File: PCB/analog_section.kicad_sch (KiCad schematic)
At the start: 75 parts, among them J3 Probe +, J4 Probe +, J5 Probe -, J6 Probe -, U1 TLV757P, U10 LM324, U3 AD9833xRM, U4 LMH6643MMX, U6 LMH6643MMX, U7 LMH6643MMX, Y1 25MHz

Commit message: Fixed some PCB bugs
The OLED display ribbon cable folded the wrong way so the screen faced
down, so I fixed that. Also made vias untented, made diodes
easier to hand solder, and added ground test hook.
The case CAD still needs to be updated.
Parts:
- D3, D4, D7, D9: footprint Diode_SMD:D_SOD-323F -> Diode_SMD:D_SOD-323_HandSoldering
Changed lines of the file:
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@@
 	(title_block
 		(title "LCR Analog Section")
-		(date "2026-05-16")
+		(date "2026-06-03")
 		(company "LWQ")
 	)
@@
 			)
 		)
-		(property "Footprint" "Diode_SMD:D_SOD-323F"
+		(property "Footprint" "Diode_SMD:D_SOD-323_HandSoldering"
 			(at 359.41 176.53 0)
 			(hide yes)
@@
 			)
 		)
-		(property "Footprint" "Diode_SMD:D_SOD-323F"
+		(property "Footprint" "Diode_SMD:D_SOD-323_HandSoldering"
 			(at 359.41 219.71 0)
 			(hide yes)
@@
 			)
 		)
-		(property "Footprint" "Diode_SMD:D_SOD-323F"
+		(property "Footprint" "Diode_SMD:D_SOD-323_HandSoldering"
 			(at 359.41 232.41 0)
 			(hide yes)
@@
 			)
 		)
-		(property "Footprint" "Diode_SMD:D_SOD-323F"
+		(property "Footprint" "Diode_SMD:D_SOD-323_HandSoldering"
 			(at 359.41 163.83 0)
 			(hide yes)

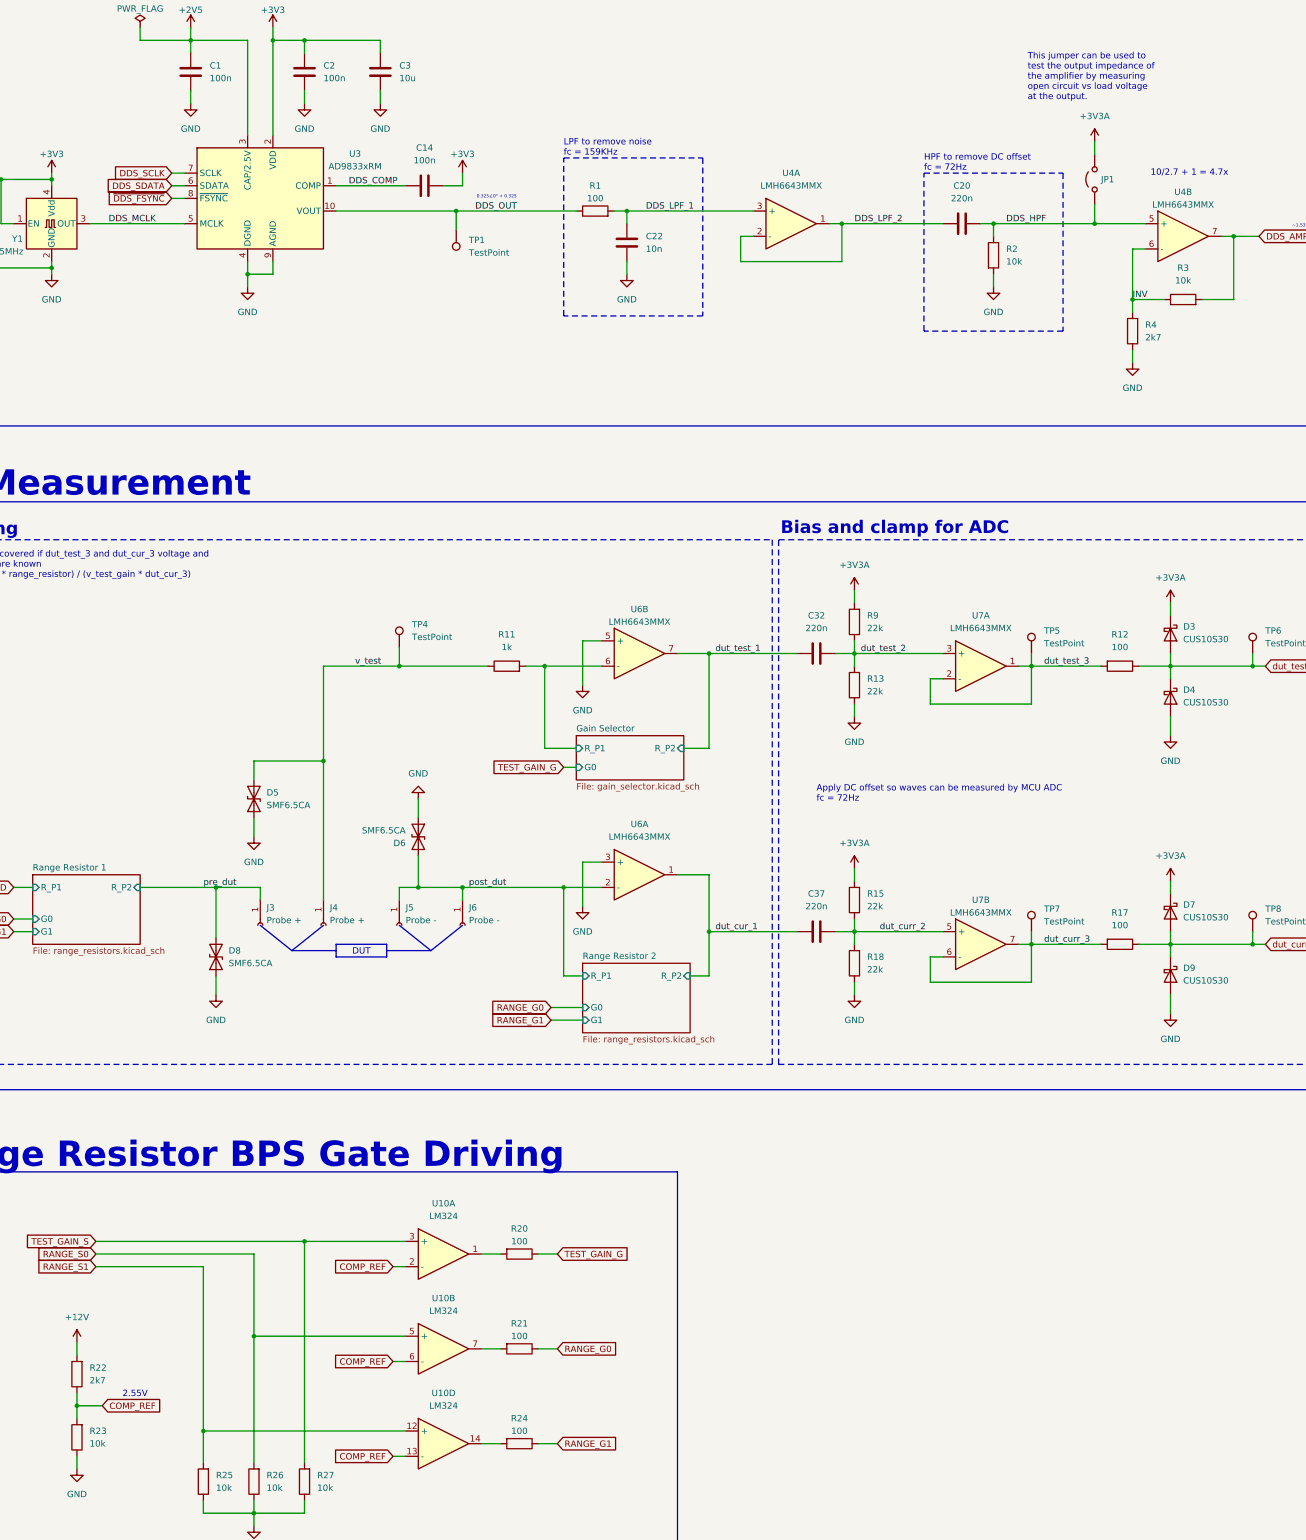
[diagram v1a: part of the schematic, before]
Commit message: Fixed gate drive comp ref
Resistors in the voltage divider were the wrong way around, now it's
correct. Also fixed the linker script, so the compiled code now uploads
to the board. Verified DDS works, and LMH6643 has 21.56 ohm output
impedance at DC. CAD still need updating.
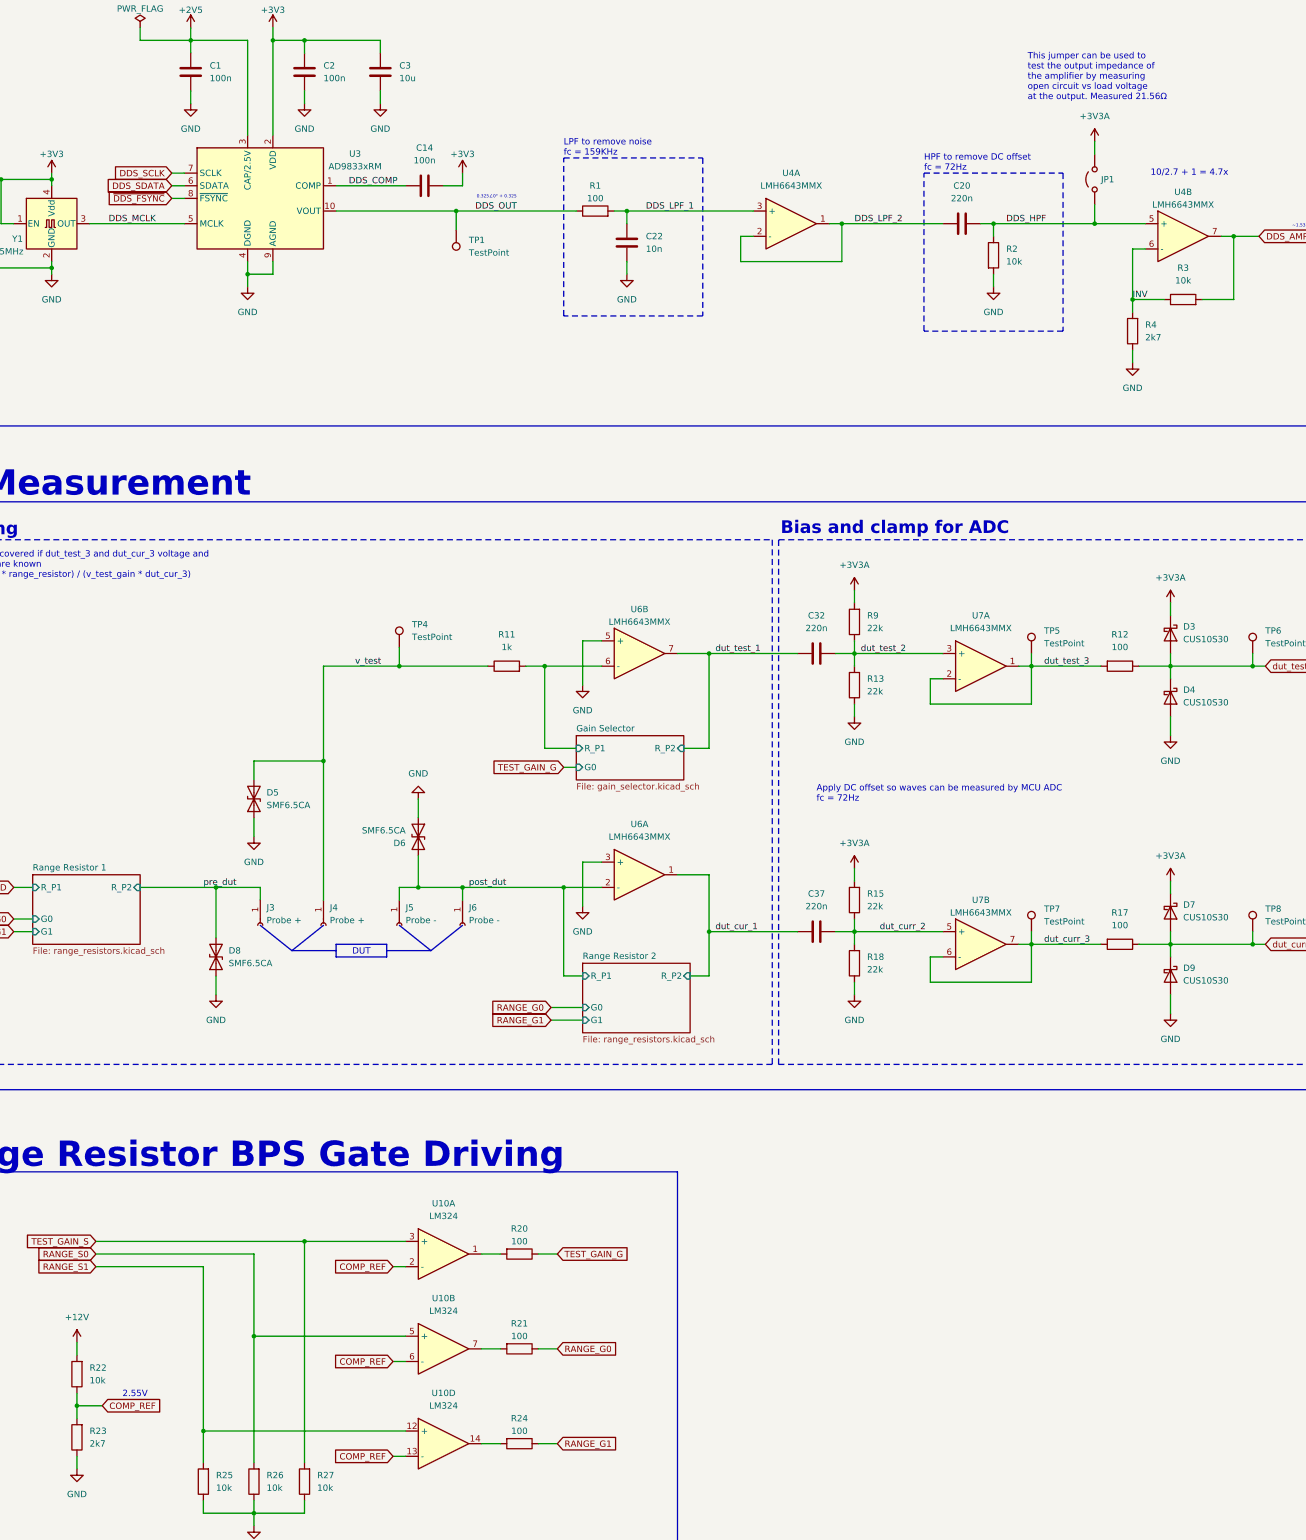
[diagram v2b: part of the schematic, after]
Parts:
- R22: value 2k7 -> 10k; Already Have 0 -> 1; LCSC PART # C114612 -> C25804
- R23: value 10k -> 2k7; Already Have 1 -> 0; LCSC PART # C25804 -> C114612
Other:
- note added: "This jumper can be used to test the output impedance of the amplifier by measuring open circuit vs load voltage at the output. Measured 21.56Ω"
- note removed: "This jumper can be used to test the output impedance of the amplifier by measuring open circuit vs load voltage at the output."
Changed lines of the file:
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@@
 		)
 	)
-	(text "This jumper can be used to\ntest the output impedance of\nthe amplifier by measuring\nopen circuit vs load voltage\nat the output."
+	(text "This jumper can be used to\ntest the output impedance of\nthe amplifier by measuring\nopen circuit vs load voltage\nat the output. Measured 21.56Ω"
 		(exclude_from_sim no)
 		(at 330.708 51.816 0)
@@
 	)
 	(symbol
-		(lib_id "Device:R")
-		(at 139.7 312.42 180)
-		(unit 1)
-		(body_style 1)
-		(exclude_from_sim no)
-		(in_bom yes)
-		(on_board yes)
-		(in_pos_files yes)
-		(dnp no)
-		(fields_autoplaced yes)
-		(property "Reference" "R22"
-			(at 142.24 311.1499 0)
-			(show_name no)
-			(do_not_autoplace no)
-			(effects
-				(font
-					(size 1.27 1.27)
-				)
-				(justify right)
-			)
-		)
-		(property "Value" "2k7"
-			(at 142.24 313.6899 0)
-			(show_name no)
-			(do_not_autoplace no)
-			(effects
-				(font
-					(size 1.27 1.27)
-				)
-				(justify right)
-			)
-		)
-		(property "Footprint" "Resistor_SMD:R_0603_1608Metric"
-			(at 141.478 312.42 90)
-			(hide yes)
-			(show_name no)
-			(do_not_autoplace no)
-			(effects
-				(font
-					(size 1.27 1.27)
-				)
-			)
-		)
-		(property "Datasheet" "https://www.lcsc.com/datasheet/C114612.pdf"
-			(at 139.7 312.42 0)
-			(hide yes)
-			(show_name no)
-			(do_not_autoplace no)
-			(effects
-				(font
-					(size 1.27 1.27)
-				)
-			)
-		)
-		(property "Description" "Resistor"
-			(at 139.7 312.42 0)
-			(hide yes)
-			(show_name no)
-			(do_not_autoplace no)
-			(effects
-				(font
-					(size 1.27 1.27)
-				)
-			)
-		)
-		(property "Already Have" "0"
-			(at 139.7 312.42 0)
-			(hide yes)
-			(show_name no)
-			(do_not_autoplace no)
-			(effects
-				(font
-					(size 1.27 1.27)
-				)
-			)
-		)
-		(property "LCSC PART #" "C114612"
-			(at 139.7 312.42 0)
-			(hide yes)
-			(show_name no)
-			(do_not_autoplace no)
-			(effects
-				(font
-					(size 1.27 1.27)
-				)
-			)
-		)
-		(pin "1"
-		)
-		(pin "2"
-		)
-		(instances
-			(project "lcr"
-				(path "/226ea51e-4da2-4daa-967e-dce167947430/c9f416db-c7a0-48f3-8fda-35fdd9af5fe5"
-					(reference "R22")
-					(unit 1)
-				)
-			)
-		)
-	)
-	(symbol
 		(lib_id "power:GND")
 		(at 458.47 76.2 180)
@@
 	(symbol
 		(lib_id "Device:R")
-		(at 139.7 325.12 180)
-		(unit 1)
-		(body_style 1)
-		(exclude_from_sim no)
-		(in_bom yes)
-		(on_board yes)
-		(in_pos_files yes)
-		(dnp no)
-		(fields_autoplaced yes)
-		(property "Reference" "R23"
-			(at 142.24 323.8499 0)
-			(show_name no)
-			(do_not_autoplace no)
-			(effects
-				(font
-					(size 1.27 1.27)
-				)
-				(justify right)
-			)
-		)
-		(property "Value" "10k"
-			(at 142.24 326.3899 0)
-			(show_name no)
-			(do_not_autoplace no)
-			(effects
-				(font
-					(size 1.27 1.27)
-				)
-				(justify right)
-			)
-		)
-		(property "Footprint" "Resistor_SMD:R_0603_1608Metric"
-			(at 141.478 325.12 90)
-			(hide yes)
-			(show_name no)
-			(do_not_autoplace no)
-			(effects
-				(font
-					(size 1.27 1.27)
-				)
-			)
-		)
-		(property "Datasheet" "https://www.lcsc.com/datasheet/C25804.pdf"
-			(at 139.7 325.12 0)
-			(hide yes)
-			(show_name no)
-			(do_not_autoplace no)
-			(effects
-				(font
-					(size 1.27 1.27)
-				)
-			)
-		)
-		(property "Description" "Resistor"
-			(at 139.7 325.12 0)
-			(hide yes)
-			(show_name no)
-			(do_not_autoplace no)
-			(effects
-				(font
-					(size 1.27 1.27)
-				)
-			)
-		)
-		(property "Already Have" "1"
-			(at 139.7 325.12 0)
-			(hide yes)
-			(show_name no)
-			(do_not_autoplace no)
-			(effects
-				(font
-					(size 1.27 1.27)
-				)
-			)
-		)
-		(property "LCSC PART #" "C25804"
-			(at 139.7 325.12 0)
-			(hide yes)
-			(show_name no)
-			(do_not_autoplace no)
-			(effects
-				(font
-					(size 1.27 1.27)
-				)
-			)
-		)
-		(pin "2"
-		)
-		(pin "1"
-		)
-		(instances
-			(project "lcr"
-				(path "/226ea51e-4da2-4daa-967e-dce167947430/c9f416db-c7a0-48f3-8fda-35fdd9af5fe5"
-					(reference "R23")
-					(unit 1)
-				)
-			)
-		)
-	)
-	(symbol
-		(lib_id "Device:R")
 		(at 165.1 334.01 180)
 		(unit 1)
@@
 	)
 	(symbol
+		(lib_id "Device:R")
+		(at 139.7 312.42 180)
+		(unit 1)
+		(body_style 1)
+		(exclude_from_sim no)
+		(in_bom yes)
+		(on_board yes)
+		(in_pos_files yes)
+		(dnp no)
+		(fields_autoplaced yes)
+		(property "Reference" "R22"
+			(at 142.24 311.1499 0)
+			(show_name no)
+			(do_not_autoplace no)
+			(effects
+				(font
+					(size 1.27 1.27)
+				)
+				(justify right)
+			)
+		)
+		(property "Value" "10k"
+			(at 142.24 313.6899 0)
+			(show_name no)
+			(do_not_autoplace no)
+			(effects
+				(font
+					(size 1.27 1.27)
+				)
+				(justify right)
+			)
+		)
+		(property "Footprint" "Resistor_SMD:R_0603_1608Metric"
+			(at 141.478 312.42 90)
+			(hide yes)
+			(show_name no)
+			(do_not_autoplace no)
+			(effects
+				(font
+					(size 1.27 1.27)
+				)
+			)
+		)
+		(property "Datasheet" "https://www.lcsc.com/datasheet/C25804.pdf"
+			(at 139.7 312.42 0)
+			(hide yes)
+			(show_name no)
+			(do_not_autoplace no)
+			(effects
+				(font
+					(size 1.27 1.27)
+				)
+			)
+		)
+		(property "Description" "Resistor"
+			(at 139.7 312.42 0)
+			(hide yes)
+			(show_name no)
+			(do_not_autoplace no)
+			(effects
+				(font
+					(size 1.27 1.27)
+				)
+			)
+		)
+		(property "Already Have" "1"
+			(at 139.7 312.42 0)
+			(hide yes)
+			(show_name no)
+			(do_not_autoplace no)
+			(effects
+				(font
+					(size 1.27 1.27)
+				)
+			)
+		)
+		(property "LCSC PART #" "C25804"
+			(at 139.7 312.42 0)
+			(hide yes)
+			(show_name no)
+			(do_not_autoplace no)
+			(effects
+				(font
+					(size 1.27 1.27)
+				)
+			)
+		)
+		(pin "2"
+		)
+		(pin "1"
+		)
+		(instances
+			(project "lcr"
+				(path "/226ea51e-4da2-4daa-967e-dce167947430/c9f416db-c7a0-48f3-8fda-35fdd9af5fe5"
+					(reference "R22")
+					(unit 1)
+				)
+			)
+		)
+	)
+	(symbol
 		(lib_id "power:+12V")
 		(at 152.4 358.14 0)
@@
 					(unit 1)
 				)
+			)
+		)
+	)
+	(symbol
+		(lib_id "Device:R")
+		(at 139.7 325.12 180)
+		(unit 1)
+		(body_style 1)
+		(exclude_from_sim no)
+		(in_bom yes)
+		(on_board yes)
+		(in_pos_files yes)
+		(dnp no)
+		(fields_autoplaced yes)
+		(property "Reference" "R23"
+			(at 142.24 323.8499 0)
+			(show_name no)
+			(do_not_autoplace no)
+			(effects
+				(font
+					(size 1.27 1.27)
+				)
+				(justify right)
+			)
+		)
+		(property "Value" "2k7"
+			(at 142.24 326.3899 0)
+			(show_name no)
+			(do_not_autoplace no)
+			(effects
+				(font
+					(size 1.27 1.27)
+				)
+				(justify right)
+			)
+		)
+		(property "Footprint" "Resistor_SMD:R_0603_1608Metric"
+			(at 141.478 325.12 90)
+			(hide yes)
+			(show_name no)
+			(do_not_autoplace no)
+			(effects
+				(font
+					(size 1.27 1.27)
+				)
+			)
+		)
+		(property "Datasheet" "https://www.lcsc.com/datasheet/C114612.pdf"
+			(at 139.7 325.12 0)
+			(hide yes)
+			(show_name no)
+			(do_not_autoplace no)
+			(effects
+				(font
+					(size 1.27 1.27)
+				)
+			)
+		)
+		(property "Description" "Resistor"
+			(at 139.7 325.12 0)
+			(hide yes)
+			(show_name no)
+			(do_not_autoplace no)
+			(effects
+				(font
+					(size 1.27 1.27)
+				)
+			)
+		)
+		(property "Already Have" "0"
+			(at 139.7 325.12 0)
+			(hide yes)
+			(show_name no)
+			(do_not_autoplace no)
+			(effects
+				(font
+					(size 1.27 1.27)
+				)
+			)
+		)
+		(property "LCSC PART #" "C114612"
+			(at 139.7 325.12 0)
+			(hide yes)
+			(show_name no)
+			(do_not_autoplace no)
+			(effects
+				(font
+					(size 1.27 1.27)
+				)
+			)
+		)
+		(pin "1"
+		)
+		(pin "2"
+		)
+		(instances
+			(project "lcr"
+				(path "/226ea51e-4da2-4daa-967e-dce167947430/c9f416db-c7a0-48f3-8fda-35fdd9af5fe5"
+					(reference "R23")
+					(unit 1)
+				)

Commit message: Range resistors now use signal relays
Most of the analog section layout was completely overhauled to fit this
change.
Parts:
- removed C43, C46: 1u, Capacitor_SMD:C_0603_1608Metric, symbol Device:C
- removed C44, C47: 100n, Capacitor_SMD:C_0603_1608Metric, symbol Device:C
- removed C45: 4u7, Capacitor_SMD:C_0603_1608Metric, symbol Device:C
- removed JP1: Jumper_2_Open, Connector_PinHeader_2.54mm:PinHeader_1x02_P2.54mm_Vertical, symbol Jumper:Jumper_2_Open
- removed PS2: A0512S-1WR2, Converter_DCDC:Converter_DCDC_XP_POWER-IAxxxxS_THT, symbol Converter_DCDC:IA2412S
- removed U10: LM324, Package_SO:SOIC-14_3.9x8.7mm_P1.27mm, symbol Device:Opamp_Quad
- added D11, D12, D13: CUS10S30, Diode_SMD:D_SOD-323_HandSoldering, symbol Device:D_Schottky
- added K1, K2, K3: G6K-2, Relay_SMD:Relay_DPDT_Omron_G6K-2F-Y, symbol Relay:G6K-2
- added Q1, Q2, Q3: NMOS, Package_TO_SOT_SMD:SOT-23-3, symbol Simulation_SPICE:NMOS
- added R28, R29, R30: 100, Resistor_SMD:R_0603_1608Metric, symbol Device:R
- added TP1, TP2, TP3, TP6, TP7, TP8: TestPoint, TestPoint:TestPoint_Pad_D1.5mm, symbol Connector:TestPoint
- added TP4: TestPoint, TestPoint:TestPoint_Keystone_5000-5004_Miniature, symbol Connector:TestPoint
- D5, D6: value SMF6.5CA -> TVS; footprint Diode_SMD:Nexperia_CFP3_SOD-123W -> Diode_SMD:D_SOD-323_HandSoldering; LCSC PART # C7466385 -> C552583
- D9: renamed from D8; value SMF6.5CA -> TVS; footprint Diode_SMD:Nexperia_CFP3_SOD-123W -> Diode_SMD:D_SOD-323_HandSoldering; LCSC PART # C7466385 -> C552583
- R20: value 100 -> 100k; Already Have 0 -> 1; LCSC PART # C105588 -> C25803
- R21: value 100 -> 5k1; Already Have 0 -> 1; LCSC PART # C105588 -> C23186
- R22, R27: value 10k -> 100k; LCSC PART # C25804 -> C25803
- R23: value 2k7 -> 5k1; Already Have 0 -> 1; LCSC PART # C114612 -> C23186
- R25: value 10k -> 100; Already Have 1 -> 0; LCSC PART # C25804 -> C105588
- renumbered D9 to D8, TP4 to TP11, TP5 to TP12, TP6 to TP13, TP7 to TP14, TP8 to TP15, TP1 to TP5
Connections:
- net DDS_AMPLIFIED is gone; now on net RANGE_1_P1: R3.2, U4.7
- net post_dut is gone; now on net RANGE_2_P1: D6.2 (A2), J5.1 (Pin_1), J6.1 (Pin_1), U6.2 (-)
- net +3V3A: now also TP1.1
- net +5V: now also D11.1 (K), D12.1 (K), D13.1 (K), K1.1, K2.1, K3.1, TP3.1
- net -3V3A: now also TP2.1
- net GND: now also Q1.3 (S), Q2.3 (S), Q3.3 (S), TP6.1, TP7.1, TP8.1; no longer R23.1, R25.1, R26.1, R27.1
- net RANGE_S0: now also R28.2; no longer R26.2
- net RANGE_S1: now also R29.2; no longer R25.2
- net TEST_GAIN_S: now also R30.2; no longer R27.2
- net RANGE_1_P1: now reaches R20.2
- net RANGE_1_P1: now also R21.2, R24.2, TP4.1
- net +12V renamed RANGE_2_P1
- net RANGE_2_P1: now also R23.2, R25.2
- net COMP_REF: no longer names the net of R22.1
- net COMP_REF: now also K1.7; no longer R23.2
- net Gain Selector/R_P1 renamed RANGE_3_P1
- net RANGE_3_P1: now also R26.2, R27.2
- net RANGE_G0: no longer names the net of R21.1
- net RANGE_G0: now also K1.4
- net RANGE_G1: no longer names the net of R24.1
- net RANGE_G1: now also K2.4
- net TEST_GAIN_G: no longer names the net of R20.1
- net TEST_GAIN_G: now also K1.2
- net dut_cur_1 renamed RANGE_2_P2
- net RANGE_2_P2: now also K1.6, K2.6
- net dut_curr_4 renamed DUT_CURR_4
- net dut_test_1 renamed RANGE_3_P2
- net RANGE_3_P2: now also K3.3
- net dut_test_4 renamed DUT_TEST_4
- net pre_dut renamed RANGE_1_P2
- net RANGE_1_P2: now also K1.3, K2.3
- net v_test renamed v_test_1
- new net: K2.5, R25.1
- new net: K3.2, R26.1
- new net: K3.4, R27.1
- new net: K1.5, R23.1
- new net COIL_D1: D11.2 (A), K1.8, Q1.1 (D)
- new net COIL_D2: D12.2 (A), K2.8, Q2.1 (D)
- new net COIL_D3: D13.2 (A), K3.8, Q3.1 (D)
- new net COIL_G1: Q1.2 (G), R28.1
- new net COIL_G2: Q2.2 (G), R29.1
- new net COIL_G3: Q3.2 (G), R30.1
- no-connect marks 0 -> 5
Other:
- removed sheet Gain Selector
- removed sheet Range Resistor 1
- removed sheet Range Resistor 2
- note added: "Component selection was based on what's cheap. If this were a real lab instrument it should probably use components that don't change with temperature (atleast in the test signal path). Average tolerances are OK, since the device needs calibration anyway."
- note added: "Main Range Resistors"
- note added: "Range Resistors"
- note added: "Test voltage gain selector"
- note added: "Testpoints"
- note removed: "2.55V"
- note removed: "Component selection was based on what's cheap. If this were a real lab instrument it should probably use components that don't change with temperature (atleast in the test signal path). Bad tolerances are OK, since the device needs calibration anyway."
- note removed: "Range Resistor BPS Gate Driving"
- note removed: "This jumper can be used to test the output impedance of the amplifier by measuring open circuit vs load voltage at the output. Measured 21.56Ω"
- moved on the sheet: D5, D6, D9, J3, J4, J5, J6, U6A
